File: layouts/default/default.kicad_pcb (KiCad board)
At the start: 2 copper layers, 48.5 x 77.2 mm, 90 parts

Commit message: What if 50x50 was enough?
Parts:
- C11, C15, C16, C17, C18, C19, C20, C21, C22, C23, C24, C25, C26, C27, C28, C29, C3, C30, C5, C6, C7, C8, R13, R14, R16, R17, R18, R19, R2, R20, R21, R22, R23, R25, R26, R28, R29, R3, R30, R31, R32, R4, R5, R6, R7, R8, R9, U4: moved to B.Cu
- moved C13 103.4 mm to (206.5, 100.8), turned to 90 degrees
- moved R10 101.1 mm to (203.2, 101.5), turned to 180 degrees
- moved C12 101.0 mm to (205.2, 102.1), turned to 90 degrees
- moved C14 99.9 mm to (206.5, 103.5), turned to -90 degrees
- moved R11 99.4 mm to (203.2, 102.8), turned to 180 degrees
- moved U3 98.5 mm to (179.5, 86.8), turned to 180 degrees
- moved U2 97.5 mm to (184.5, 88.2), turned to 0 degrees
- moved R1 94.0 mm to (188.2, 84.8), turned to 0 degrees
- moved R12 92.4 mm to (188.5, 95.0), turned to 90 degrees
- moved C4 89.0 mm to (185.5, 78.2), turned to 90 degrees
- moved C2 87.0 mm to (179.0, 108.5), turned to 90 degrees
- moved L1 86.3 mm to (179.9, 95.7), turned to 180 degrees
- moved C11 81.1 mm to (179.0, 93.0), turned to 0 degrees
- moved C25 80.7 mm to (200.7, 94.3), turned to -90 degrees
- moved R22 80.6 mm to (198.5, 93.6)
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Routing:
- net SCL: track 80.3 -> 0.00 mm, vias 1 -> 0
- net SDA: track 76.4 -> 0.00 mm, vias 1 -> 0
- net -gnd: track 75.7 -> 0.00 mm, vias 35 -> 0
- net pack-gnd-0: track 31.9 -> 5.14 mm, vias 13 -> 0
- net pack-SRN: track 26.1 -> 0.00 mm
- net vbat: track 25.2 -> 0.00 mm, vias 4 -> 0
- net pack-SRP: track 24.5 -> 0.00 mm
- net CHG: track 21.1 -> 0.00 mm, vias 3 -> 0
- net pack-gnd-2: track 29.0 -> 8.55 mm
- net REGN: track 19.5 -> 0.00 mm, vias 2 -> 0
- net pack-anode: track 19.4 -> 0.00 mm, vias 2 -> 0
- net charger-D: track 18.5 -> 0.00 mm
- net -pos: track 18.2 -> 0.00 mm
- net charger-G-3: track 18.2 -> 0.00 mm, vias 2 -> 0
- net charger-G-2: track 18.0 -> 0.00 mm, vias 2 -> 0
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- added copper zone on In1.Cu, net -gnd
- removed copper zone on B.Cu, net -gnd
- removed copper zone on F.Cu, net -gnd
- removed copper zone on F.Cu, net -pos
- removed copper zone on F.Cu, net S
- removed copper zone on F.Cu, net charger-D
- removed copper zone on F.Cu, net charger-pos-0
- removed copper zone on F.Cu, net charger-pos-2
- removed copper zone on F.Cu, net pack-D-0
- removed copper zone on F.Cu, net pack-D-1
- removed copper zone on B.Cu, net pack-gnd-0
- removed copper zone on F.Cu, net pack-gnd-0
- removed copper zone on F.Cu, net vbat
- removed copper zone on F.Cu, net vsys
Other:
- board size 48.5 x 77.2 mm -> 50 x 50 mm
- copper layers 2 -> 4

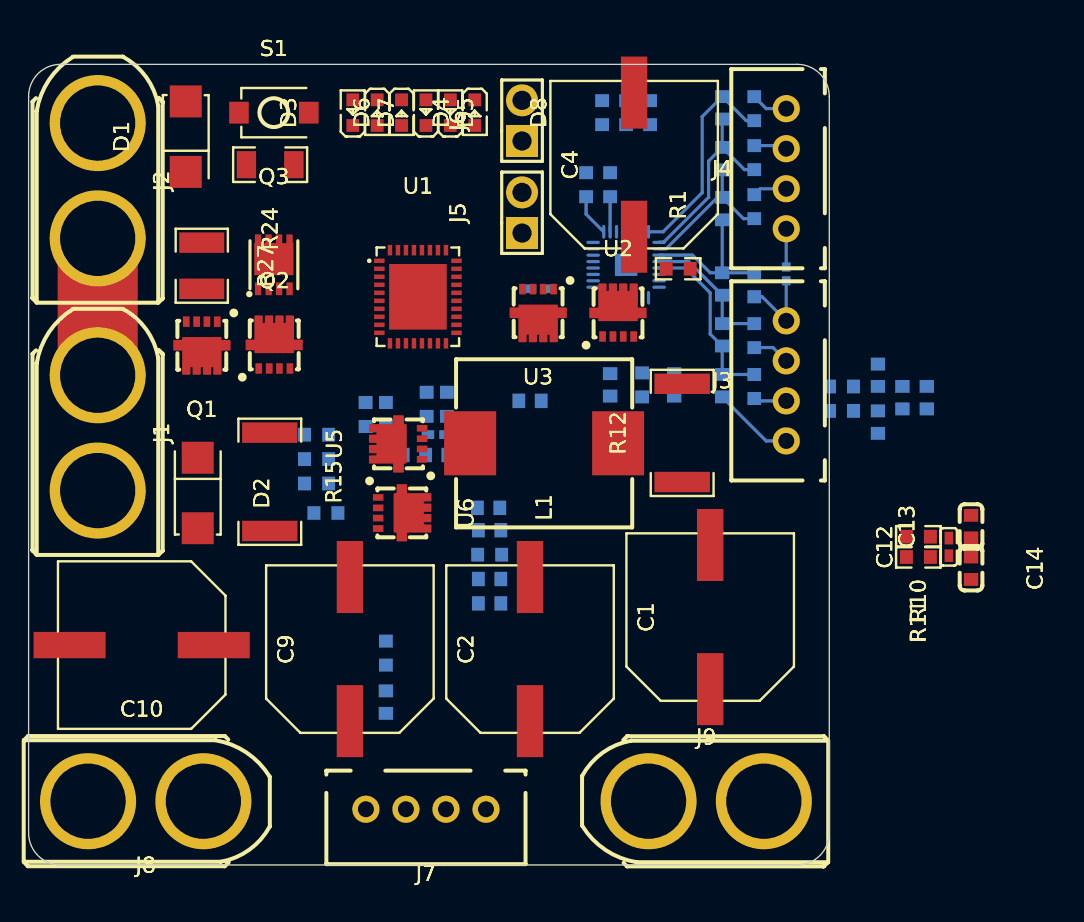
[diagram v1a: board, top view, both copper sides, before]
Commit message: Try out a 4 layer stackup within 50x50
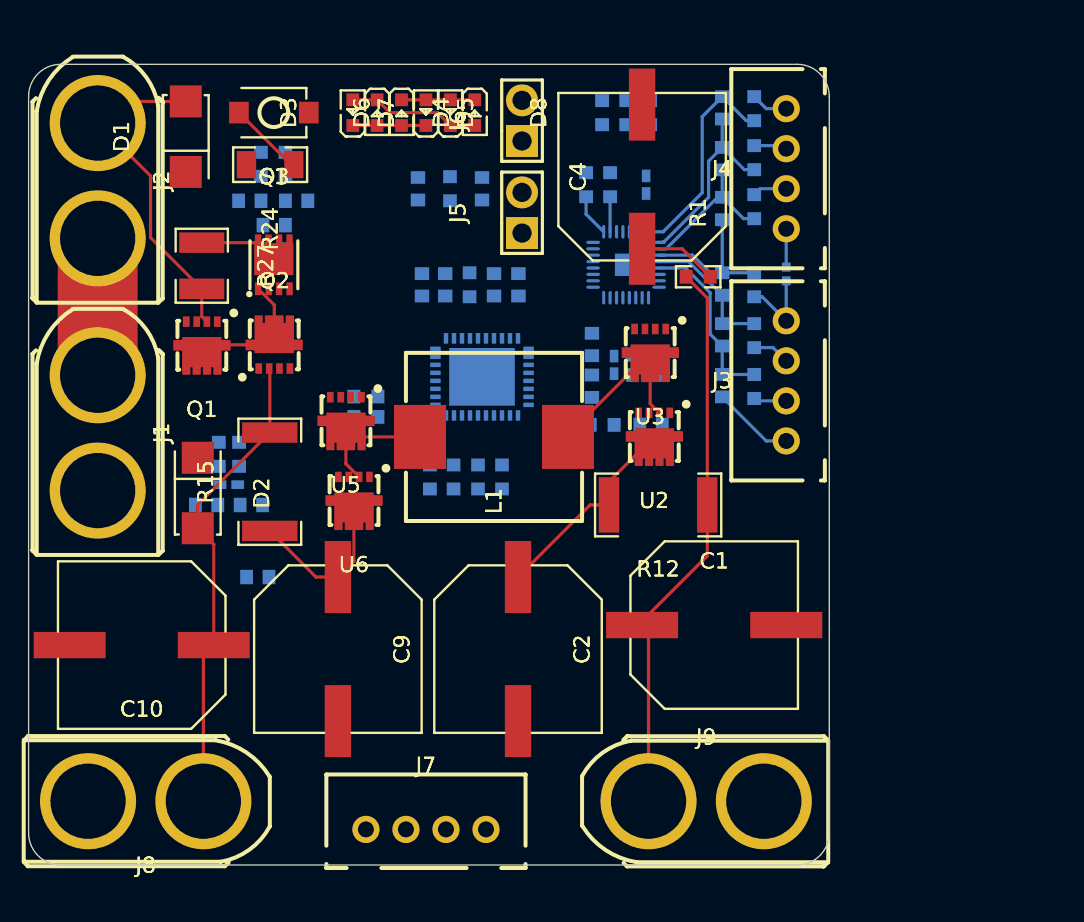
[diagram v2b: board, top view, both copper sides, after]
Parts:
- C12, C13, C14, R10, R11, U1: moved to B.Cu
- moved C29 41.8 mm to (163.0, 83.5), turned to 180 degrees
- moved C25 41.6 mm to (161.5, 80.5), turned to 180 degrees
- moved C24 40.7 mm to (163.0, 82.0), turned to 180 degrees
- moved R22 39.4 mm to (162.2, 78.2), turned to 90 degrees
- moved C26 37.9 mm to (164.4, 80.5), turned to 0 degrees
- moved R23 37.4 mm to (163.7, 78.2), turned to 90 degrees
- moved C14 26.3 mm to (182.9, 92.1)
- moved C13 26.3 mm to (182.9, 89.5)
- moved C3 24.0 mm to (186.6, 94.5), turned to 180 degrees
- moved C12 23.8 mm to (184.2, 90.8)
- moved R10 20.5 mm to (186.2, 90.1), turned to 0 degrees
- moved R11 20.5 mm to (186.2, 91.4), turned to 0 degrees
- moved C11 20.2 mm to (162.0, 104.0)
- moved C6 20.0 mm to (178.3, 85.8), turned to -90 degrees
- moved R5 19.6 mm to (183.5, 94.5), turned to 0 degrees
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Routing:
- net -pos: track 0.00 -> 35.1 mm
- net vsys: track 0.00 -> 29.6 mm
- net vbat: track 0.00 -> 21.3 mm
- net charger-pos-0: track 0.00 -> 13.0 mm
- net S: track 0.00 -> 11.4 mm
- net charger-pos-2: track 0.00 -> 10.6 mm
- net charger-D: track 0.00 -> 8.88 mm
- net pack-D-0: track 0.00 -> 8.46 mm
- net pack-anode: track 0.00 -> 8.28 mm
- net charger-pos-1: track 0.00 -> 4.97 mm
- net pack-D-1: track 0.00 -> 4.93 mm
- net pack-gnd-0: track 5.14 -> 9.92 mm
- net pack-cathode-3: track 0.00 -> 4.57 mm
- net pack-cathode-2: track 0.00 -> 4.57 mm
